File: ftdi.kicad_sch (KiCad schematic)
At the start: 31 parts, among them U1301 AT93C56, U1302 FT2232HL, Y1301 12MHz CL=18p

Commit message: FTDI: add extra decoupling
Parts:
- added C1315: 100n, Capacitor_SMD:C_0805_2012Metric, symbol Device:C
- renumbered C1304 to C1303, C1303 to C1304, C1306 to C1305, C1305 to C1306, C1310 to C1307, C1307 to C1308, C1308 to C1309, C1309 to C1310, C1314 to C1311, C1311 to C1312, C1312 to C1313, C1313 to C1314
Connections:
- net FT_+3V3 is gone; now on net FT_3V3: R1311.2
- net FT_3V3: now also C1315.1
- net GND: now also C1315.2
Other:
- moved on the sheet: C1303, C1305, C1307, C1311

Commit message: FT2232H: pull BCBUS2&3 high
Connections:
- net at R1311.1, U1302.53 (BCBUS2): now also U1302.54 (BCBUS3)
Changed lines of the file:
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@@
   (junction (at 76.2 123.19) (diameter 0) (color 0 0 0 0)
   )
+  (junction (at 172.72 125.73) (diameter 0) (color 0 0 0 0)
+  )
   (junction (at 48.26 81.28) (diameter 0) (color 0 0 0 0)
   )
@@
     (stroke (width 0) (type default) (color 0 0 0 0))
   )
+  (wire (pts (xy 172.72 125.73) (xy 173.99 125.73))
+    (stroke (width 0) (type default) (color 0 0 0 0))
+  )
   (wire (pts (xy 97.79 140.97) (xy 97.79 147.32))
     (stroke (width 0) (type default) (color 0 0 0 0))
@@
     (stroke (width 0) (type default) (color 0 0 0 0))
   )
+  (wire (pts (xy 171.45 128.27) (xy 172.72 128.27))
+    (stroke (width 0) (type default) (color 0 0 0 0))
+  )
   (wire (pts (xy 171.45 77.47) (xy 187.96 77.47))
     (stroke (width 0) (type default) (color 0 0 0 0))
@@
     (stroke (width 0) (type default) (color 0 0 0 0))
   )
-  (wire (pts (xy 171.45 125.73) (xy 173.99 125.73))
-    (stroke (width 0) (type default) (color 0 0 0 0))
-  )
+  (wire (pts (xy 171.45 125.73) (xy 172.72 125.73))
+    (stroke (width 0) (type default) (color 0 0 0 0))
+  )
+  (wire (pts (xy 172.72 125.73) (xy 172.72 128.27))
+    (stroke (width 0) (type default) (color 0 0 0 0))
+  )

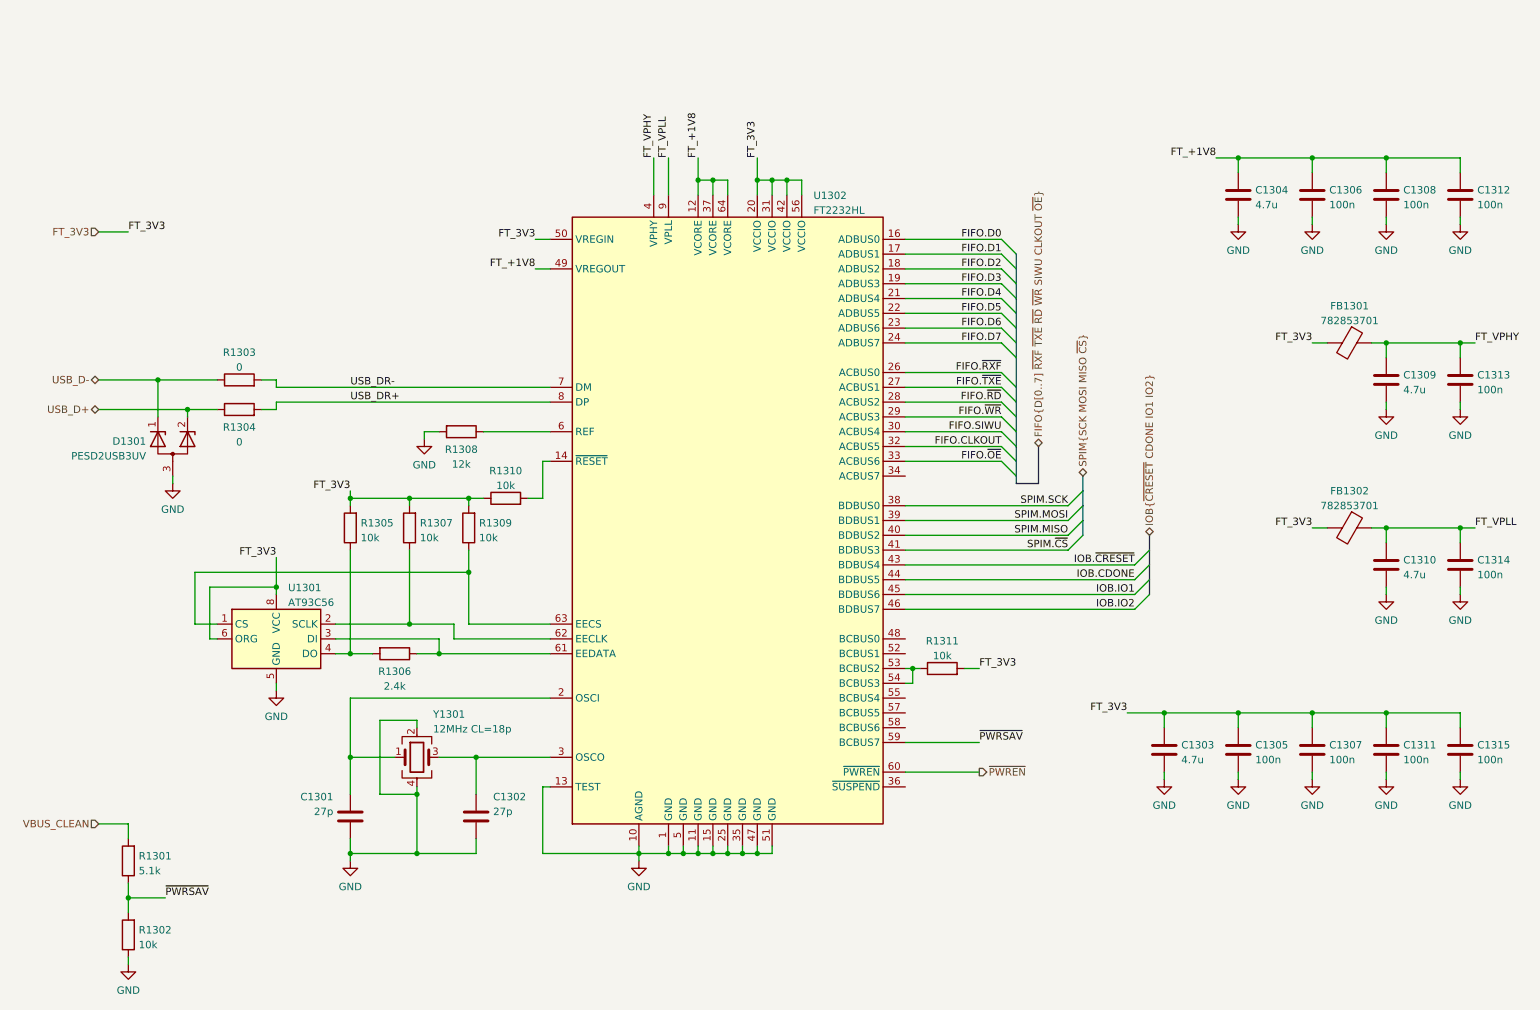
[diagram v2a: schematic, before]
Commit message: Update schematic: - Redesign of decoupling based on swcad modelling (predominantly use 1uf, no paralleled caps) - Reroute REF_CLK_IN, CLK_SEL net to different FPGA pins - Some net renaming - Ext conn: add decoupling to 3v3 output - Reassign references to all components PCB: routing almost finished
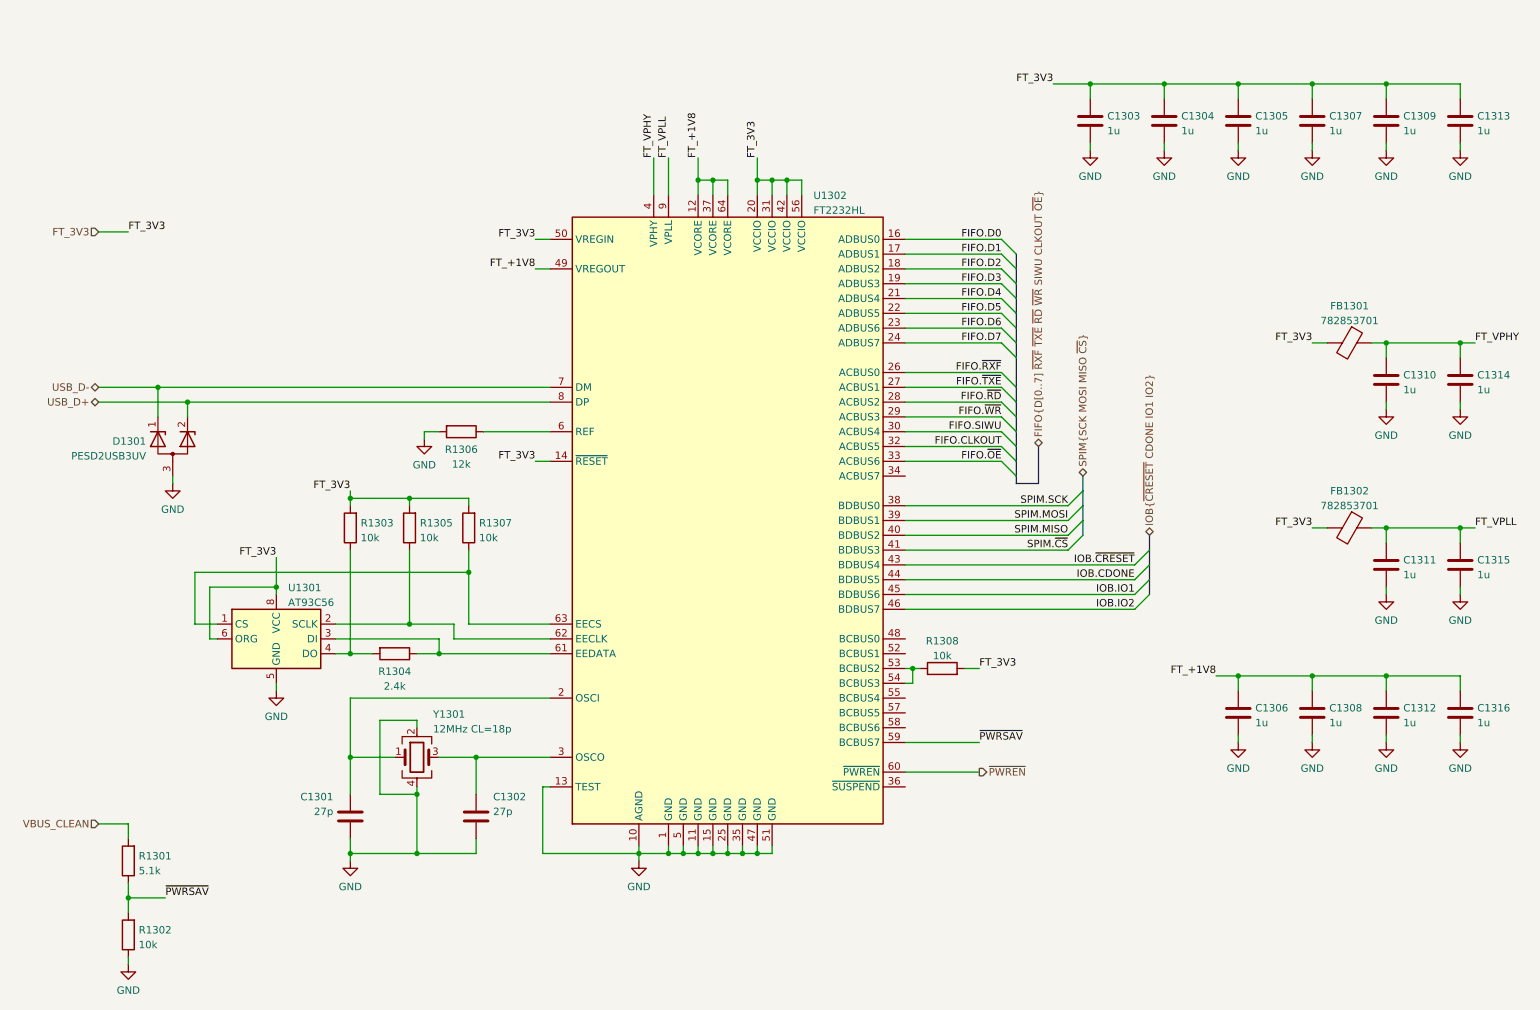
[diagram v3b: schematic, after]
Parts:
- removed R1303, R1304: 0, Resistor_SMD:R_0805_2012Metric, symbol Device:R
- removed R1310: 10k, Resistor_SMD:R_0805_2012Metric, symbol Device:R
- added C1316: 1u, Capacitor_SMD:C_0805_2012Metric, symbol Device:C
- C1303, C1304, C1309, C1310: value 4.7u -> 1u; Mfr Murata -> Samsung; Mfr PN GRM21BR71C475ME51 -> CL21B105KOFNNNG
- C1305, C1306, C1307, C1308, C1311, C1312, C1313, C1314, C1315: value 100n -> 1u; Mfr PN CL21B104KBFNNNE -> CL21B105KOFNNNG
- renumbered R1305 to R1303, R1306 to R1304, R1307 to R1305, R1308 to R1306, R1309 to R1307, R1311 to R1308
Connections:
- net USB_DR+ is gone; now on net USB_D+: U1302.8 (DP)
- net USB_DR- is gone; now on net USB_D-: U1302.7 (DM)
- net FT_+1V8: now also C1316.1; no longer C1304.1
- net FT_3V3: now also C1304.1, C1309.1, C1313.1, U1302.14 (~{RESET}); no longer C1311.1, C1315.1
- net FT_VPHY: now also C1310.1, C1314.1; no longer C1309.1, C1313.1
- net FT_VPLL: now also C1311.1, C1315.1; no longer C1310.1, C1314.1
- net GND: now also C1316.2
